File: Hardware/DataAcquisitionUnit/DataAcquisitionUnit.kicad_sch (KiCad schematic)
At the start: 0 parts

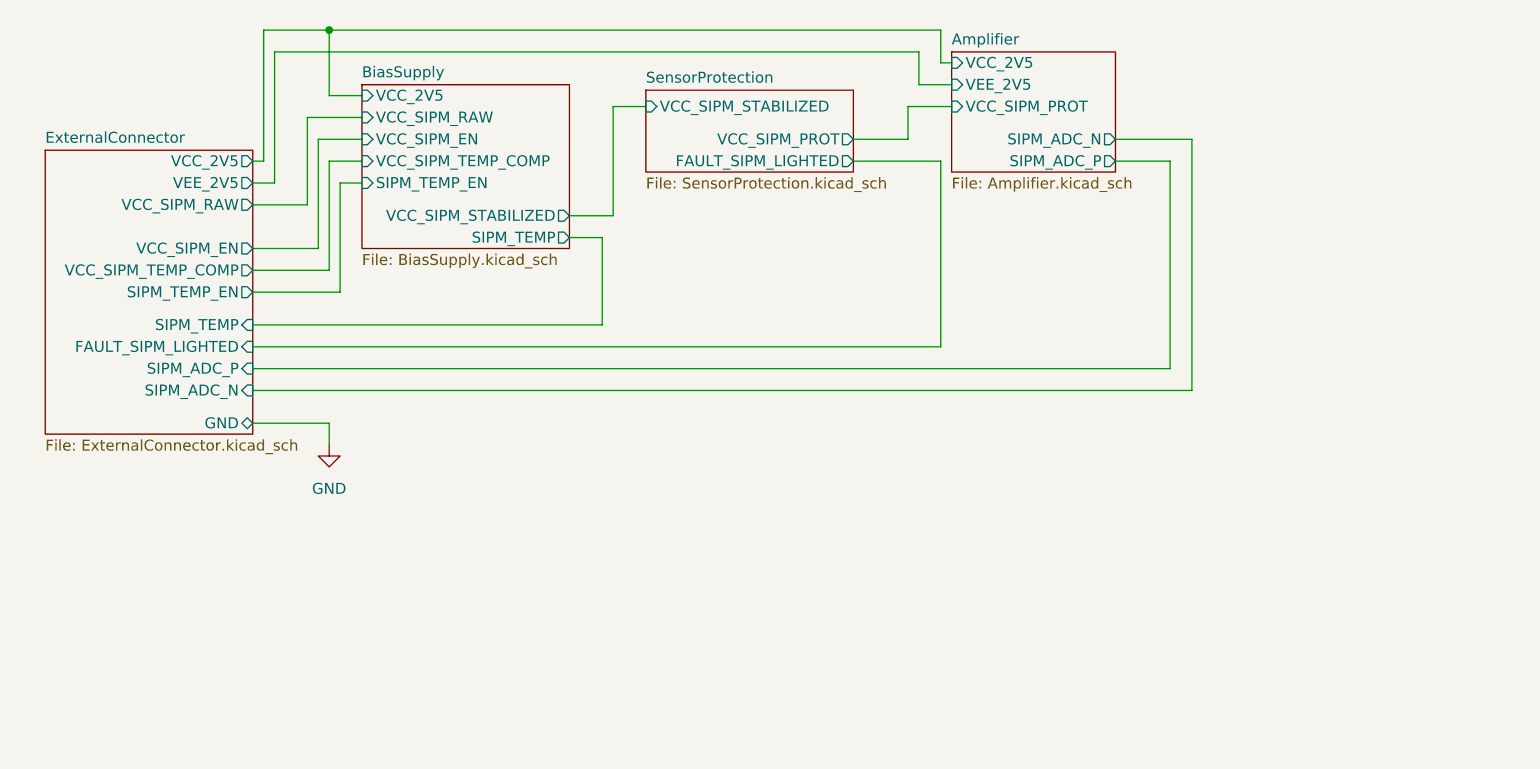
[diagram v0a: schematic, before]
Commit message: fix: #129, fix: #127
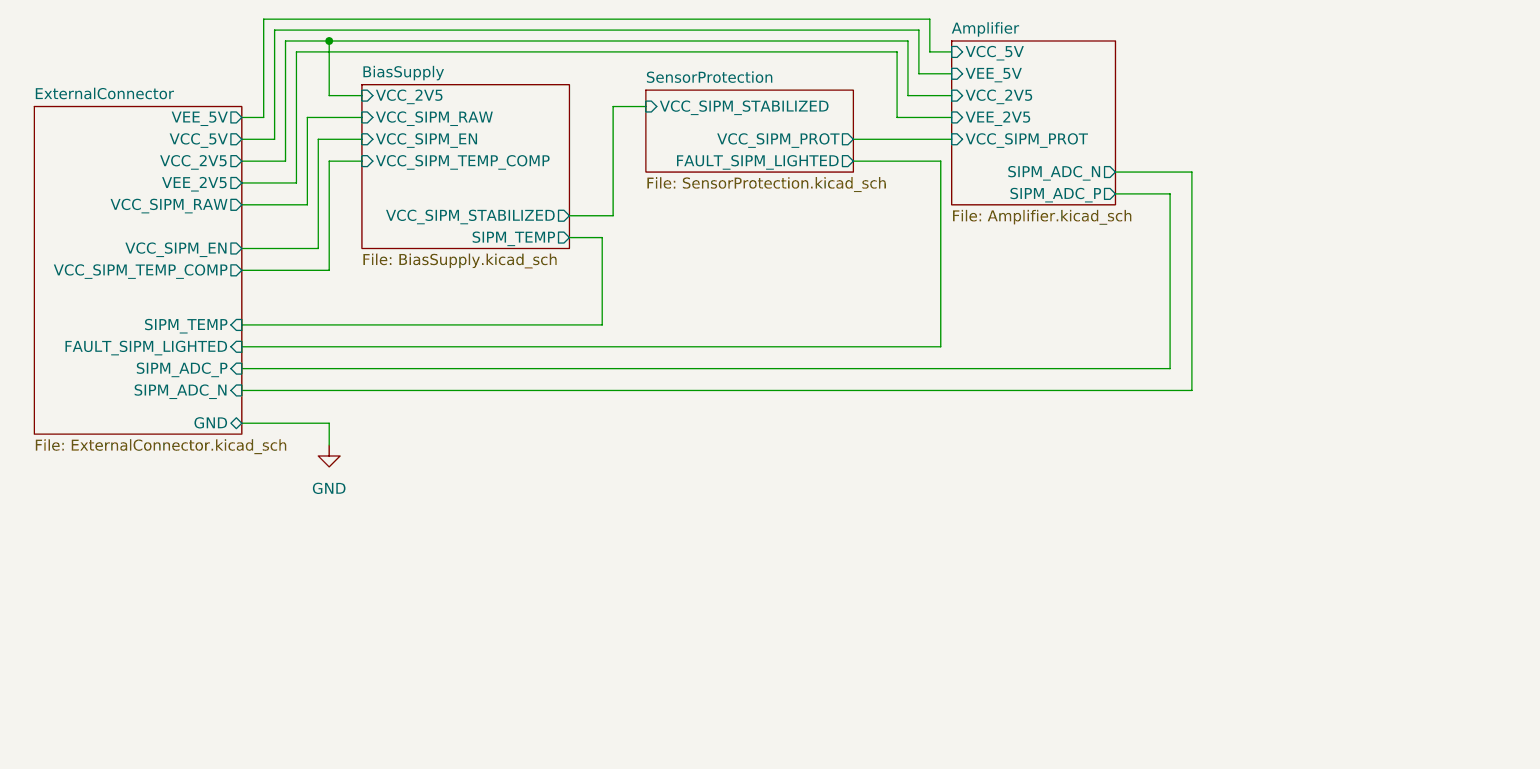
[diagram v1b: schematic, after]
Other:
- sheet Amplifier ports: added VCC_5V, VEE_5V; removed none
- sheet BiasSupply ports: added none; removed SIPM_TEMP_EN
- sheet ExternalConnector ports: added VCC_5V, VEE_5V; removed SIPM_TEMP_EN

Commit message: fix: #132
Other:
- added sheet ADC (ADC.kicad_sch)
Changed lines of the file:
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@@
+	)
+	(sheet
+		(at 214.63 109.22)
+		(size 12.7 3.81)
+		(exclude_from_sim no)
+		(in_bom yes)
+		(on_board yes)
+		(dnp no)
+		(fields_autoplaced yes)
+		(stroke
+			(width 0.1524)
+			(type solid)
+		)
+		(fill
+			(color 0 0 0 0)
+		)
+		(property "Sheetname" "ADC"
+			(at 214.63 108.5084 0)
+			(show_name no)
+			(do_not_autoplace no)
+			(effects
+				(font
+					(size 1.27 1.27)
+				)
+				(justify left bottom)
+			)
+		)
+		(property "Sheetfile" "ADC.kicad_sch"
+			(at 214.63 113.6146 0)
+			(show_name no)
+			(do_not_autoplace no)
+			(effects
+				(font
+					(size 1.27 1.27)
+				)
+				(justify left top)
+			)
+		)
+		(instances
+			(project "DataAcquisitionUnit"
+				(path "/b3e88616-4405-48d6-aecf-2659499541fb"
+					(page "5")
+				)
+			)
+		)
 	)
 	(sheet
